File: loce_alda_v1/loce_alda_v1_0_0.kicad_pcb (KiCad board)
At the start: 2 copper layers, 223.3 x 88.9 mm, 94 parts, among them J1 batt_jst_conn, J15 extra_btn, J16 extra_btn, J17 TP_thumb_r, J18 TP_thumb, J19 TP_index_r, J20 TP_index, J21 batt_jst_conn_r, J3 track_point_left, J4 niceview_left, J5 niceview_right, J6 track_point_right, SW1 SW_Push, SW10 SW_Push, SW10_r1 SW_Push, SW11 SW_Push, SW11_r1 SW_Push, SW12 SW_Push, SW12_r1 SW_Push, SW13 SW_Push, SW13_r1 SW_Push, SW14 SW_Push, SW14_r1 SW_Push, SW15 SW_Push, SW15_r1 SW_Push, SW16 SW_Push, SW16_r1 SW_Push, SW17 SW_Push, SW17_r1 SW_Push, SW1_r1 SW_Push, SW2 SW_Push, SW2_r1 SW_Push, SW3 SW_Push, SW3_r1 SW_Push, SW4 SW_Push, SW4_r1 SW_Push, SW5 SW_Push, SW5_r1 SW_Push, SW6 SW_Push, SW6_r1 SW_Push, SW7 SW_Push, SW7_r1 SW_Push, SW8 SW_Push, SW8_r1 SW_Push, SW9 SW_Push, SW9_r1 SW_Push, U1 SeeeduinoXIAO_BLE, U2 SeeeduinoXIAO_BLE, U3 74HC595, U4 74HC595

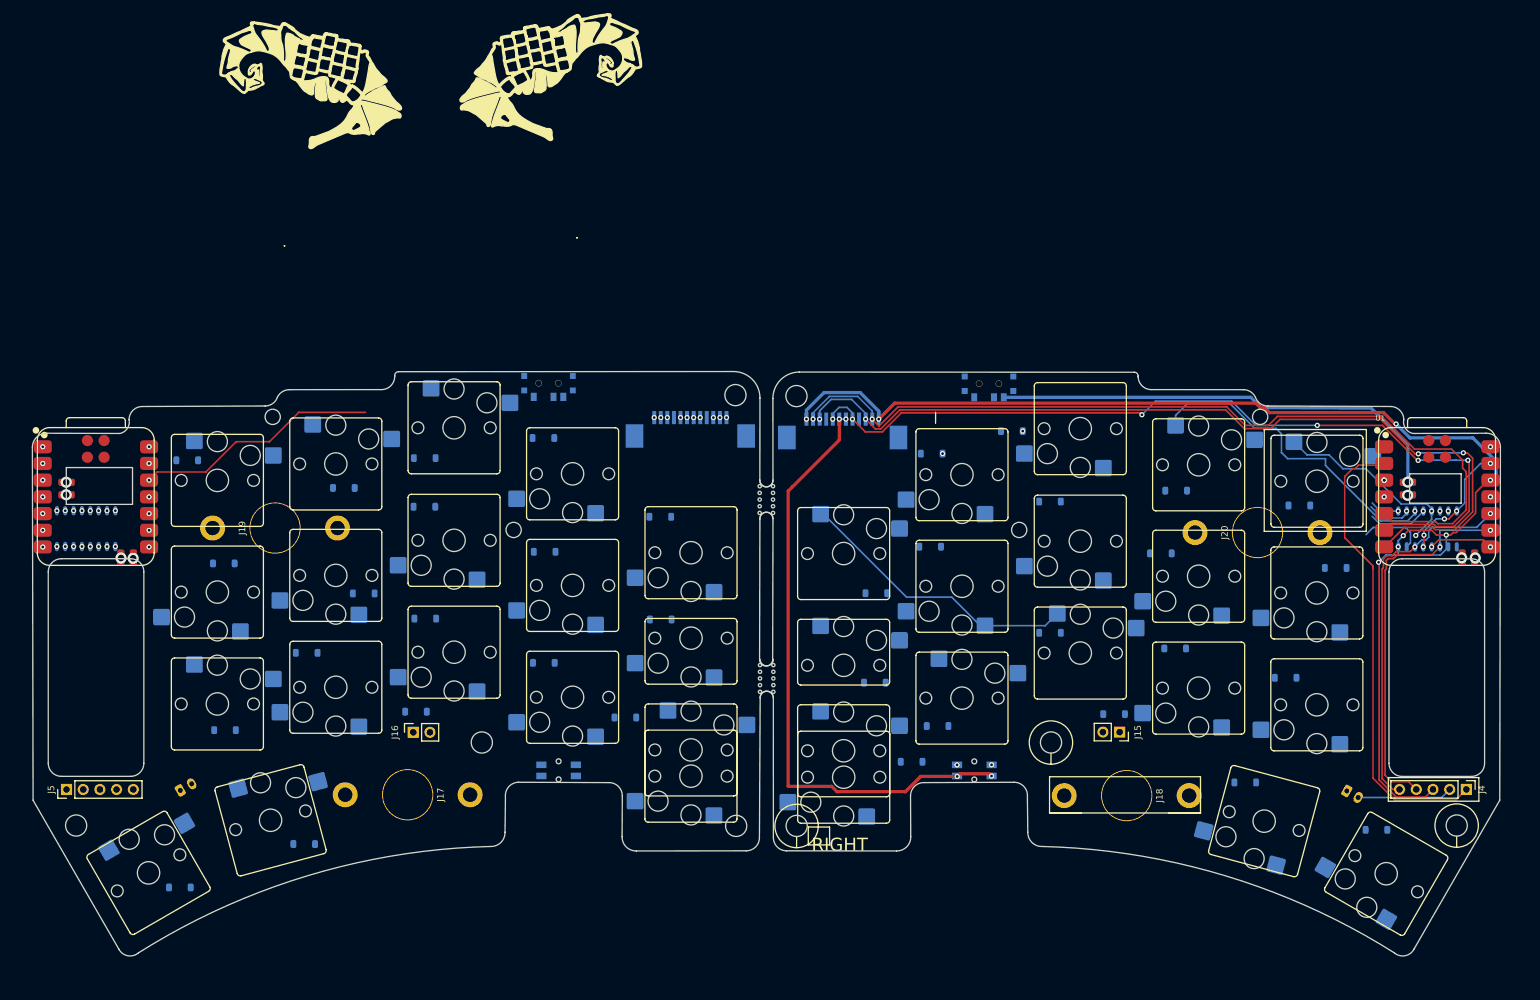
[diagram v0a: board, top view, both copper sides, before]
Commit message: feat: more routing
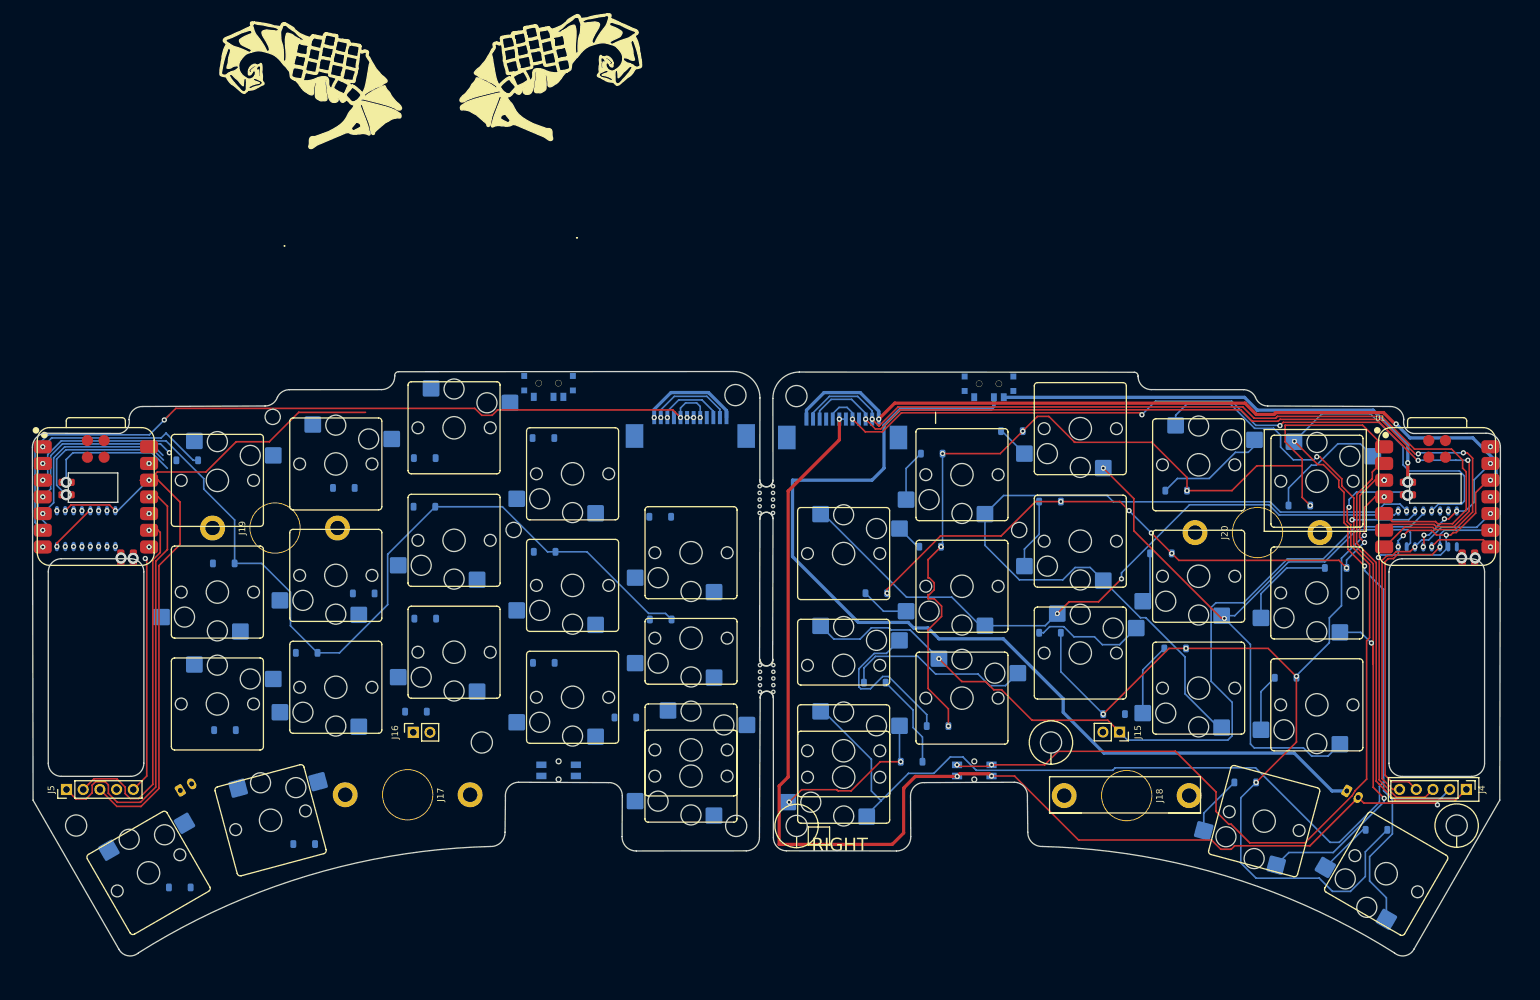
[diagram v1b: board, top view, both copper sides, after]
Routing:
- net COL4: track 30.6 -> 235.8 mm, vias 2 -> 3
- net BT+: track 0.00 -> 152.4 mm
- net ROW2: track 0.00 -> 146.5 mm, vias 1 -> 6
- net ROW1_r: track 0.00 -> 141.9 mm
- net ROW0: track 0.00 -> 141.6 mm, vias 2 -> 6
- net reset: track 0.00 -> 129.7 mm, vias 3 -> 4
- net IPD_CLK_r: track 0.00 -> 122.7 mm, vias 3 -> 4
- net COL5: track 9.09 -> 130.9 mm, vias 1 -> 2
- net COL1: track 6.78 -> 124.8 mm
- net ROW1: track 0.00 -> 111.7 mm, vias 2 -> 9
- net vcc_r: track 37.2 -> 131.6 mm, vias 5 -> 4
- net COL2: track 9.99 -> 103.9 mm, vias 0 -> 2
- net gnd: track 126.0 -> 208.2 mm
- net COL3: track 49.8 -> 125.9 mm, vias 1 -> 5
- net MOSI_r: track 0.00 -> 65.8 mm
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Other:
- outline, holes or cut-outs redrawn

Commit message: feat: wire the loce alda
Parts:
- added G***: LOGO, LOGO, F.Cu at (103.1, 103.5)
- added G***: LOGO, LOGO, F.Cu at (195.3, 103.8)
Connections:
- J1 pad 1: BT+_r -> gnd_r
- J1 pad 2: gnd_r -> BT+_r
- J21 pad 1: BT+ -> gnd
- J21 pad 2: gnd -> BT+
- U2 pad 16: BT+_r -> raw_r
- U2 pad 17: nfc_2_r -> unconnected-(U2-J13-pin_2-Pad17)
- U2 pad 18: nfc_1_r -> unconnected-(U2-J13-pin_1-Pad18)
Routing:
- net gnd_r: track 8.64 -> 348.0 mm, vias 5 -> 11
- net COL4_r: track 0.00 -> 214.5 mm, vias 1 -> 5
- net ROW2_r: track 26.1 -> 212.0 mm, vias 2 -> 4
- net COL5_r: track 0.00 -> 142.9 mm
- net COL2_r: track 0.00 -> 141.0 mm, vias 1 -> 4
- net BT+_r: track 20.2 -> 145.9 mm, vias 1 -> 2
- net ROW0_r: track 26.2 -> 149.6 mm, vias 1 -> 3
- net COL0_r: track 0.00 -> 122.2 mm, vias 1 -> 5
- net COL1_r: track 0.00 -> 119.7 mm, vias 1 -> 4
- net IPD_RST_r: track 10.3 -> 126.1 mm, vias 2 -> 1
- net COL3_r: track 0.00 -> 112.3 mm, vias 1 -> 3
- net reset_r: track 23.5 -> 130.8 mm, vias 1 -> 3
- net Net-(D27-A): track 0.00 -> 98.2 mm
- net Net-(D28-A): track 0.00 -> 94.0 mm, vias 0 -> 2
- net raw_r: track 0.00 -> 91.9 mm, vias 0 -> 3
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- added copper zone on B.Cu, net gnd
- added copper zone on F.Cu, net gnd
- added copper zone on B.Cu, net gnd_r
- added copper zone on F.Cu, net gnd_r
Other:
- outline, holes or cut-outs redrawn
- board text added: "+"
- board text added: "-"

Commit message: feat:
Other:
- board text added: "Left"
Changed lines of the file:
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@@
+		)
+	)
+	(gr_text "Left"
+		(at 168.76 105.63 0)
+		(layer "B.SilkS")
+		(effects
+			(font
+				(size 2 2)
+				(thickness 0.15)
+			)
+			(justify left bottom mirror)
 		)
 	)
